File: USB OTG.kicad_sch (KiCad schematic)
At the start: 24 parts, among them J2 USB_OTG, Q1 Q_PNP_BEC, U1 rv1126/rv1109

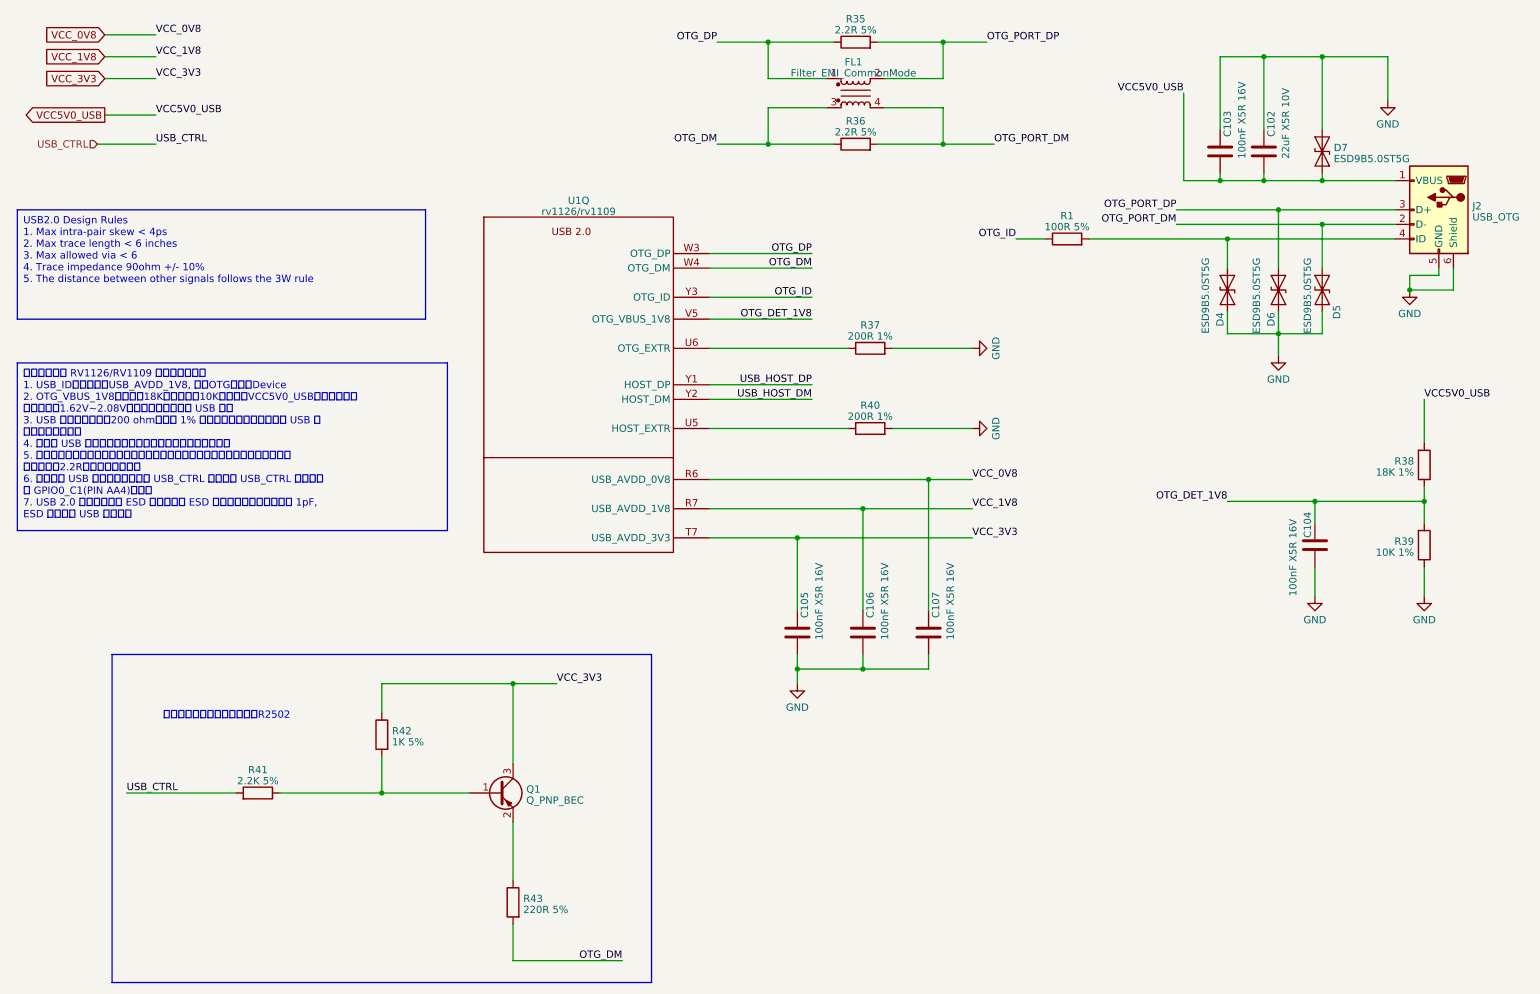
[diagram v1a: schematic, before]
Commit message: updated footprints
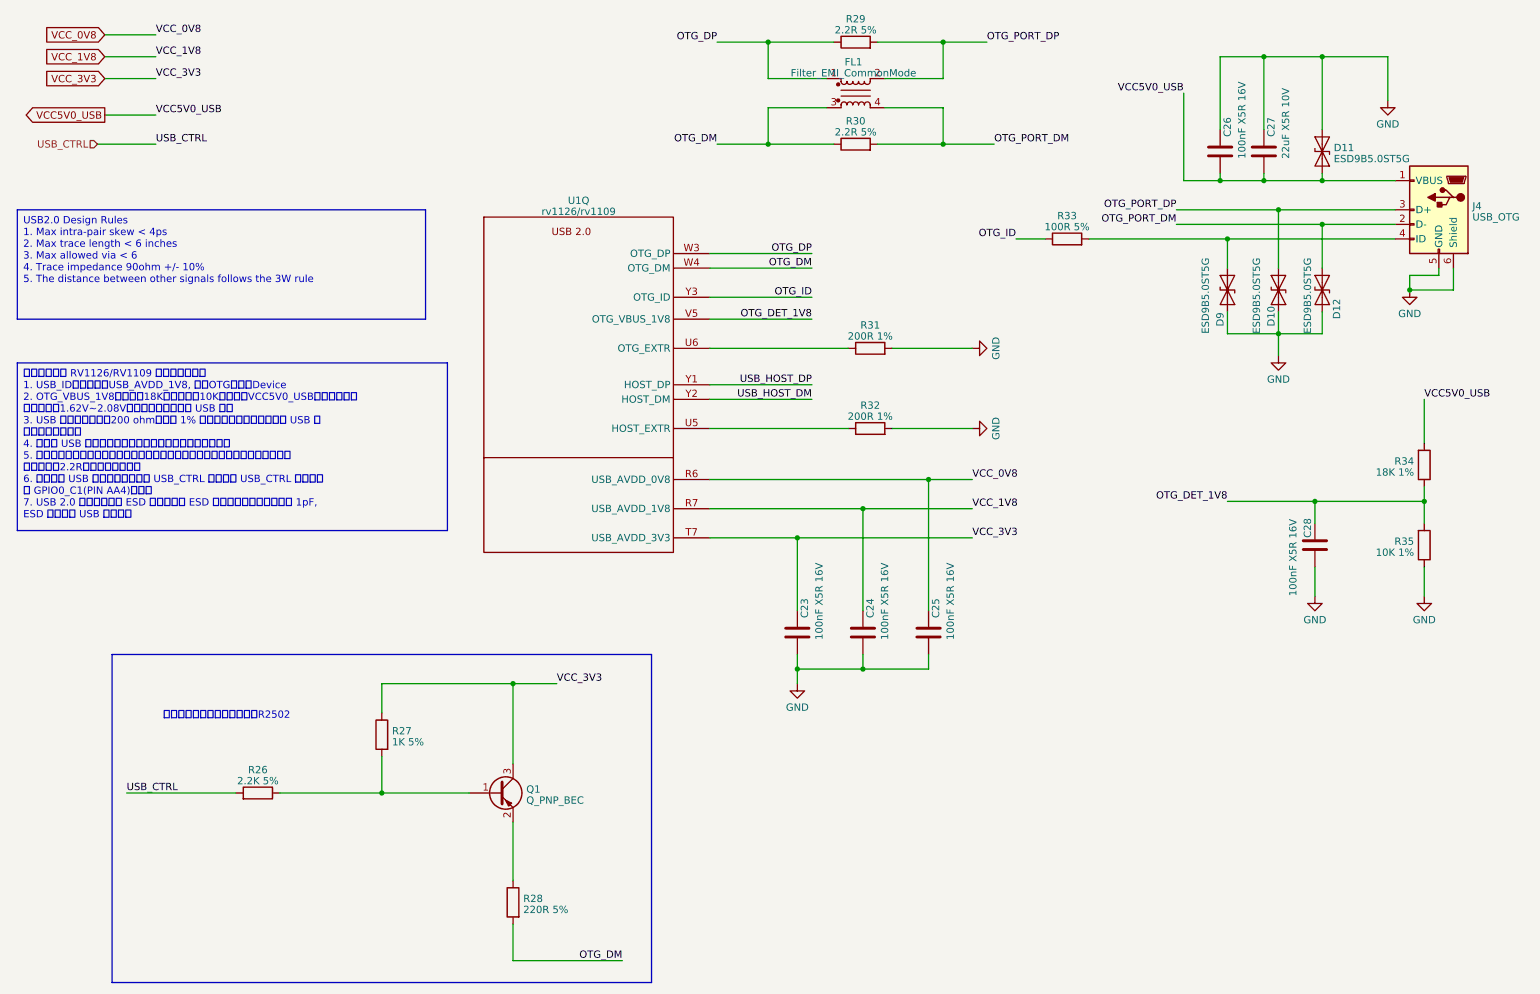
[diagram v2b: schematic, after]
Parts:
- U1: footprint (none) -> Rockchip_SoC:Rockchip_RV1126_FCCSP409LD_14.0x14.0mm
- renumbered C105 to C23, C106 to C24, C107 to C25, C103 to C26, C102 to C27, C104 to C28, D6 to D10, D7 to D11, D5 to D12, D4 to D9, J2 to J4, R41 to R26, R42 to R27, R43 to R28, R35 to R29, R36 to R30, R37 to R31, R40 to R32, R1 to R33, R38 to R34, R39 to R35

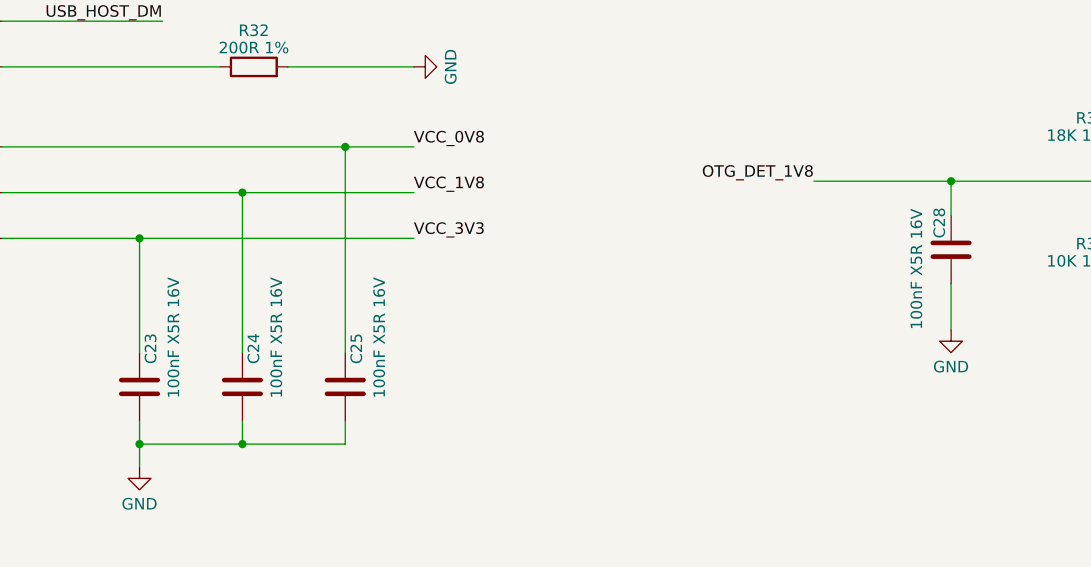
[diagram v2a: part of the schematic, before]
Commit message: updated Capacitors
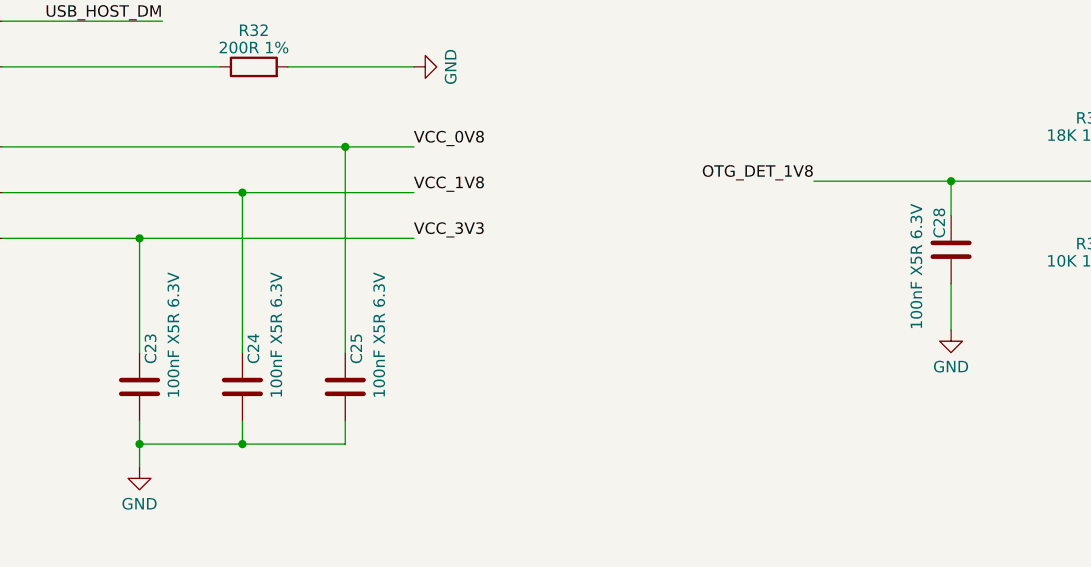
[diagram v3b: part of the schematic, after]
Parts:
- C23, C24, C25: value 100nF X5R 16V -> 100nF X5R 6.3V; LCSC (none) -> C76934; Model (none) -> GRM033R61A104KE15D; Vendor (none) -> muRata(村田)
- C28: value 100nF X5R 16V -> 100nF X5R 6.3V; footprint Capacitor_SMD:C_0402_1005Metric -> Capacitor_SMD:C_0201_0603Metric; LCSC (none) -> C76934; Model (none) -> GRM033R61A104KE15D; Vendor (none) -> muRata(村田)
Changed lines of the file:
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@@
       (effects (font (size 1.27 1.27)) (justify left))
     )
-    (property "Value" "100nF X5R 16V" (at 167.64 125.73 90)
+    (property "Value" "100nF X5R 6.3V" (at 167.64 125.73 90)
       (effects (font (size 1.27 1.27)) (justify left))
     )
@@
     )
     (property "Datasheet" "~" (at 163.83 124.46 0)
+      (effects (font (size 1.27 1.27)) hide)
+    )
+    (property "Description" "容值: 100nF 精度: ±10% 额定电压: 10V 材质(温度系数): X5R 材质:X5R" (at 163.83 124.46 0)
+      (effects (font (size 1.27 1.27)) hide)
+    )
+    (property "Model" "GRM033R61A104KE15D" (at 163.83 124.46 0)
+      (effects (font (size 1.27 1.27)) hide)
+    )
+    (property "Vendor" "muRata(村田)" (at 163.83 124.46 0)
+      (effects (font (size 1.27 1.27)) hide)
+    )
+    (property "LCSC" "C76934" (at 163.83 124.46 0)
       (effects (font (size 1.27 1.27)) hide)
     )
@@
       (effects (font (size 1.27 1.27)) (justify left))
     )
-    (property "Value" "100nF X5R 16V" (at 238.76 118.11 90)
-      (effects (font (size 1.27 1.27)) (justify left))
-    )
-    (property "Footprint" "Capacitor_SMD:C_0402_1005Metric" (at 236.22 114.3 0)
+    (property "Value" "100nF X5R 6.3V" (at 238.76 118.11 90)
+      (effects (font (size 1.27 1.27)) (justify left))
+    )
+    (property "Footprint" "Capacitor_SMD:C_0201_0603Metric" (at 236.22 114.3 0)
       (effects (font (size 1.27 1.27)) hide)
     )
     (property "Datasheet" "~" (at 242.57 109.22 0)
+      (effects (font (size 1.27 1.27)) hide)
+    )
+    (property "Description" "容值: 100nF 精度: ±10% 额定电压: 10V 材质(温度系数): X5R 材质:X5R" (at 242.57 109.22 0)
+      (effects (font (size 1.27 1.27)) hide)
+    )
+    (property "LCSC" "C76934" (at 242.57 109.22 0)
+      (effects (font (size 1.27 1.27)) hide)
+    )
+    (property "Model" "GRM033R61A104KE15D" (at 242.57 109.22 0)
+      (effects (font (size 1.27 1.27)) hide)
+    )
+    (property "Vendor" "muRata(村田)" (at 242.57 109.22 0)
       (effects (font (size 1.27 1.27)) hide)
     )
@@
       (effects (font (size 1.27 1.27)) (justify left))
     )
-    (property "Value" "100nF X5R 16V" (at 156.21 125.73 90)
+    (property "Value" "100nF X5R 6.3V" (at 156.21 125.73 90)
       (effects (font (size 1.27 1.27)) (justify left))
     )
@@
     )
     (property "Datasheet" "~" (at 152.4 124.46 0)
+      (effects (font (size 1.27 1.27)) hide)
+    )
+    (property "Description" "容值: 100nF 精度: ±10% 额定电压: 10V 材质(温度系数): X5R 材质:X5R" (at 152.4 124.46 0)
+      (effects (font (size 1.27 1.27)) hide)
+    )
+    (property "Model" "GRM033R61A104KE15D" (at 152.4 124.46 0)
+      (effects (font (size 1.27 1.27)) hide)
+    )
+    (property "Vendor" "muRata(村田)" (at 152.4 124.46 0)
+      (effects (font (size 1.27 1.27)) hide)
+    )
+    (property "LCSC" "C76934" (at 152.4 124.46 0)
       (effects (font (size 1.27 1.27)) hide)
     )
@@
       (effects (font (size 1.27 1.27)) (justify left))
     )
-    (property "Value" "100nF X5R 16V" (at 179.07 125.73 90)
+    (property "Value" "100nF X5R 6.3V" (at 179.07 125.73 90)
       (effects (font (size 1.27 1.27)) (justify left))
     )
@@
       (effects (font (size 1.27 1.27)) hide)
     )
+    (property "Description" "容值: 100nF 精度: ±10% 额定电压: 10V 材质(温度系数): X5R 材质:X5R" (at 175.26 124.46 0)
+      (effects (font (size 1.27 1.27)) hide)
+    )
+    (property "Model" "GRM033R61A104KE15D" (at 175.26 124.46 0)
+      (effects (font (size 1.27 1.27)) hide)
+    )
+    (property "Vendor" "muRata(村田)" (at 175.26 124.46 0)
+      (effects (font (size 1.27 1.27)) hide)
+    )
+    (property "LCSC" "C76934" (at 175.26 124.46 0)
+      (effects (font (size 1.27 1.27)) hide)
+    )

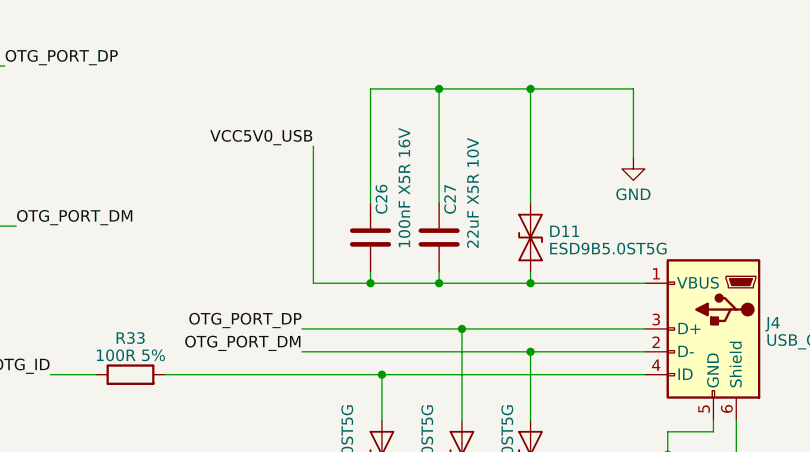
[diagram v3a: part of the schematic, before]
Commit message: updated LCSC selection of capacitors
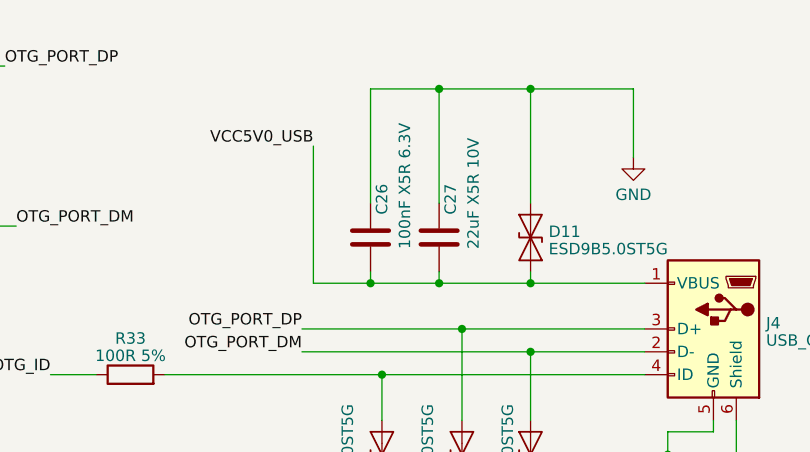
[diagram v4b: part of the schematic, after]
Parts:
- C26: value 100nF X5R 16V -> 100nF X5R 6.3V; footprint Capacitor_SMD:C_0402_1005Metric -> Capacitor_SMD:C_0201_0603Metric; LCSC (none) -> C76934; Model (none) -> GRM033R61A104KE15D; Vendor (none) -> muRata(村田)
- C27: footprint Capacitor_SMD:C_0805_2012Metric -> Capacitor_SMD:C_0603_1608Metric; LCSC (none) -> C162690; Model (none) -> ZRB18AR61A226ME01L; Vendor (none) -> muRata(村田)
- J4: footprint (none) -> Connector_USB:USB_Micro-B_Amphenol_10118194_Horizontal
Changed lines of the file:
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@@
       (effects (font (size 1.27 1.27)) (justify right))
     )
-    (property "Footprint" "" (at 260.35 52.07 0)
+    (property "Footprint" "Connector_USB:USB_Micro-B_Amphenol_10118194_Horizontal" (at 260.35 52.07 0)
       (effects (font (size 1.27 1.27)) hide)
     )
@@
       (effects (font (size 1.27 1.27)) (justify left))
     )
-    (property "Value" "100nF X5R 16V" (at 229.87 41.91 90)
-      (effects (font (size 1.27 1.27)) (justify left))
-    )
-    (property "Footprint" "Capacitor_SMD:C_0402_1005Metric" (at 232.41 45.72 0)
+    (property "Value" "100nF X5R 6.3V" (at 229.87 41.91 90)
+      (effects (font (size 1.27 1.27)) (justify left))
+    )
+    (property "Footprint" "Capacitor_SMD:C_0201_0603Metric" (at 232.41 45.72 0)
       (effects (font (size 1.27 1.27)) hide)
     )
     (property "Datasheet" "~" (at 226.06 40.64 0)
+      (effects (font (size 1.27 1.27)) hide)
+    )
+    (property "Description" "容值: 100nF 精度: ±10% 额定电压: 10V 材质(温度系数): X5R 材质:X5R" (at 226.06 40.64 0)
+      (effects (font (size 1.27 1.27)) hide)
+    )
+    (property "Model" "GRM033R61A104KE15D" (at 226.06 40.64 0)
+      (effects (font (size 1.27 1.27)) hide)
+    )
+    (property "Vendor" "muRata(村田)" (at 226.06 40.64 0)
+      (effects (font (size 1.27 1.27)) hide)
+    )
+    (property "LCSC" "C76934" (at 226.06 40.64 0)
       (effects (font (size 1.27 1.27)) hide)
     )
@@
       (effects (font (size 1.27 1.27)) (justify left))
     )
-    (property "Footprint" "Capacitor_SMD:C_0805_2012Metric" (at 234.6452 44.45 0)
+    (property "Footprint" "Capacitor_SMD:C_0603_1608Metric" (at 234.6452 44.45 0)
       (effects (font (size 1.27 1.27)) hide)
     )
@@
       (effects (font (size 1.27 1.27)) hide)
     )
+    (property "Description" "容值: 22uF 精度: ±20% 额定电压: 10V 材质(温度系数): X5R 材质：X5R" (at 233.68 40.64 0)
+      (effects (font (size 1.27 1.27)) hide)
+    )
+    (property "LCSC" "C162690" (at 233.68 40.64 0)
+      (effects (font (size 1.27 1.27)) hide)
+    )
+    (property "Model" "ZRB18AR61A226ME01L" (at 233.68 40.64 0)
+      (effects (font (size 1.27 1.27)) hide)
+    )
+    (property "Vendor" "muRata(村田)" (at 233.68 40.64 0)
+      (effects (font (size 1.27 1.27)) hide)
+    )

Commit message: layout SoC Power and DDR capacitors
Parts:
- C23, C24, C25, C26, C28: LCSC C76934 -> C76928; Model GRM033R61A104KE15D -> GRM033R60J104KE19D
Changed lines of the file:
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@@
       (effects (font (size 1.27 1.27)) hide)
     )
-    (property "Description" "容值: 100nF 精度: ±10% 额定电压: 10V 材质(温度系数): X5R 材质:X5R" (at 163.83 124.46 0)
-      (effects (font (size 1.27 1.27)) hide)
-    )
-    (property "Model" "GRM033R61A104KE15D" (at 163.83 124.46 0)
+    (property "Description" "容值: 100nF 精度: ±10% 额定电压: 6.3V 材质(温度系数): X5R 材质:X5R" (at 163.83 124.46 0)
+      (effects (font (size 1.27 1.27)) hide)
+    )
+    (property "Model" "GRM033R60J104KE19D" (at 163.83 124.46 0)
       (effects (font (size 1.27 1.27)) hide)
     )
@@
       (effects (font (size 1.27 1.27)) hide)
     )
-    (property "LCSC" "C76934" (at 163.83 124.46 0)
+    (property "LCSC" "C76928" (at 163.83 124.46 0)
       (effects (font (size 1.27 1.27)) hide)
     )
@@
       (effects (font (size 1.27 1.27)) hide)
     )
-    (property "Description" "容值: 100nF 精度: ±10% 额定电压: 10V 材质(温度系数): X5R 材质:X5R" (at 242.57 109.22 0)
-      (effects (font (size 1.27 1.27)) hide)
-    )
-    (property "LCSC" "C76934" (at 242.57 109.22 0)
-      (effects (font (size 1.27 1.27)) hide)
-    )
-    (property "Model" "GRM033R61A104KE15D" (at 242.57 109.22 0)
+    (property "Description" "容值: 100nF 精度: ±10% 额定电压: 6.3V 材质(温度系数): X5R 材质:X5R" (at 242.57 109.22 0)
+      (effects (font (size 1.27 1.27)) hide)
+    )
+    (property "LCSC" "C76928" (at 242.57 109.22 0)
+      (effects (font (size 1.27 1.27)) hide)
+    )
+    (property "Model" "GRM033R60J104KE19D" (at 242.57 109.22 0)
       (effects (font (size 1.27 1.27)) hide)
     )
@@
       (effects (font (size 1.27 1.27)) hide)
     )
-    (property "Description" "容值: 100nF 精度: ±10% 额定电压: 10V 材质(温度系数): X5R 材质:X5R" (at 152.4 124.46 0)
-      (effects (font (size 1.27 1.27)) hide)
-    )
-    (property "Model" "GRM033R61A104KE15D" (at 152.4 124.46 0)
+    (property "Description" "容值: 100nF 精度: ±10% 额定电压: 6.3V 材质(温度系数): X5R 材质:X5R" (at 152.4 124.46 0)
+      (effects (font (size 1.27 1.27)) hide)
+    )
+    (property "Model" "GRM033R60J104KE19D" (at 152.4 124.46 0)
       (effects (font (size 1.27 1.27)) hide)
     )
@@
       (effects (font (size 1.27 1.27)) hide)
     )
-    (property "LCSC" "C76934" (at 152.4 124.46 0)
+    (property "LCSC" "C76928" (at 152.4 124.46 0)
       (effects (font (size 1.27 1.27)) hide)
     )
@@
       (effects (font (size 1.27 1.27)) hide)
     )
-    (property "Description" "容值: 100nF 精度: ±10% 额定电压: 10V 材质(温度系数): X5R 材质:X5R" (at 226.06 40.64 0)
-      (effects (font (size 1.27 1.27)) hide)
-    )
-    (property "Model" "GRM033R61A104KE15D" (at 226.06 40.64 0)
+    (property "Description" "容值: 100nF 精度: ±10% 额定电压: 6.3V 材质(温度系数): X5R 材质:X5R" (at 226.06 40.64 0)
+      (effects (font (size 1.27 1.27)) hide)
+    )
+    (property "Model" "GRM033R60J104KE19D" (at 226.06 40.64 0)
       (effects (font (size 1.27 1.27)) hide)
     )
@@
       (effects (font (size 1.27 1.27)) hide)
     )
-    (property "LCSC" "C76934" (at 226.06 40.64 0)
+    (property "LCSC" "C76928" (at 226.06 40.64 0)
       (effects (font (size 1.27 1.27)) hide)
     )
@@
       (effects (font (size 1.27 1.27)) hide)
     )
-    (property "Description" "容值: 100nF 精度: ±10% 额定电压: 10V 材质(温度系数): X5R 材质:X5R" (at 175.26 124.46 0)
-      (effects (font (size 1.27 1.27)) hide)
-    )
-    (property "Model" "GRM033R61A104KE15D" (at 175.26 124.46 0)
+    (property "Description" "容值: 100nF 精度: ±10% 额定电压: 6.3V 材质(温度系数): X5R 材质:X5R" (at 175.26 124.46 0)
+      (effects (font (size 1.27 1.27)) hide)
+    )
+    (property "Model" "GRM033R60J104KE19D" (at 175.26 124.46 0)
       (effects (font (size 1.27 1.27)) hide)
     )
@@
       (effects (font (size 1.27 1.27)) hide)
     )
-    (property "LCSC" "C76934" (at 175.26 124.46 0)
-      (effects (font (size 1.27 1.27)) hide)
-    )
+    (property "LCSC" "C76928" (at 175.26 124.46 0)
+      (effects (font (size 1.27 1.27)) hide)
+    )

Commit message: updated Resistors
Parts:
- R26: LCSC (none) -> C966701; Model (none) -> CQ02WGJ0222TCE; Vendor (none) -> UNI-ROYAL(厚声)
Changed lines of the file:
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@@
+      (effects (font (size 1.27 1.27)) hide)
+    )
+    (property "Description" "阻值: 2.2kΩ 精度: ±5% 功率: 0.0625W 温度系数: ±100ppm/℃" (at 58.42 152.4 0)
+      (effects (font (size 1.27 1.27)) hide)
+    )
+    (property "LCSC" "C966701" (at 58.42 152.4 0)
+      (effects (font (size 1.27 1.27)) hide)
+    )
+    (property "Model" "CQ02WGJ0222TCE" (at 58.42 152.4 0)
+      (effects (font (size 1.27 1.27)) hide)
+    )
+    (property "Vendor" "UNI-ROYAL(厚声)" (at 58.42 152.4 0)
       (effects (font (size 1.27 1.27)) hide)
     )
